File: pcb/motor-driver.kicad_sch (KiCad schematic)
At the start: 14 parts, among them J3 B6B-PH-SM4-TB, U7 TMC2130-LA

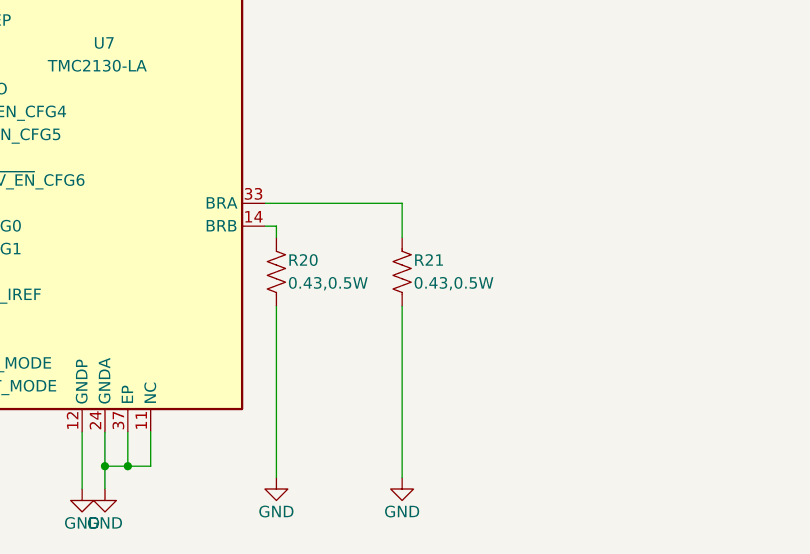
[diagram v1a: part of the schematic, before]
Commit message: Change Rsense to 0.47 Ohms
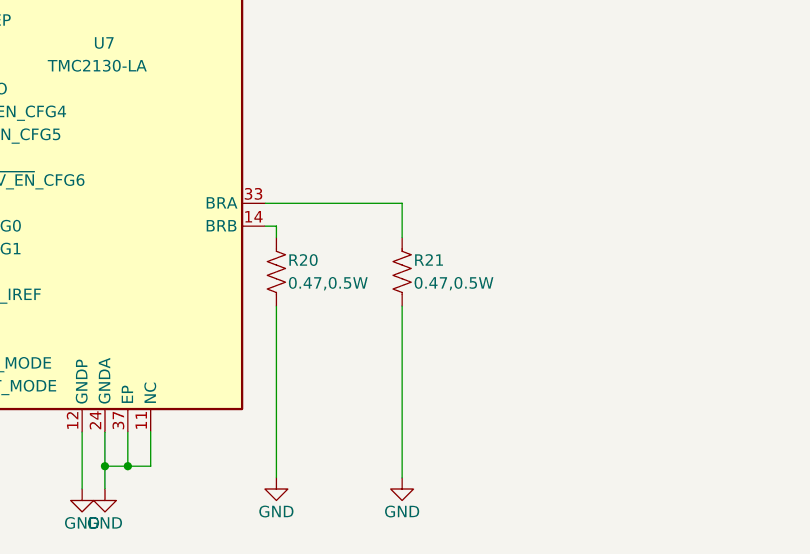
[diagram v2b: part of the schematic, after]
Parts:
- R20, R21: value 0.43,0.5W -> 0.47,0.5W
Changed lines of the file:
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@@
 			)
 		)
-		(property "Value" "0.43,0.5W"
+		(property "Value" "0.47,0.5W"
 			(at 182.88 124.46 0)
 			(effects
@@
 			)
 		)
-		(property "Value" "0.43,0.5W"
+		(property "Value" "0.47,0.5W"
 			(at 168.91 124.46 0)
 			(effects
